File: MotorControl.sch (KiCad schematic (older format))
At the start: 2 parts, among them U3 74LVC125

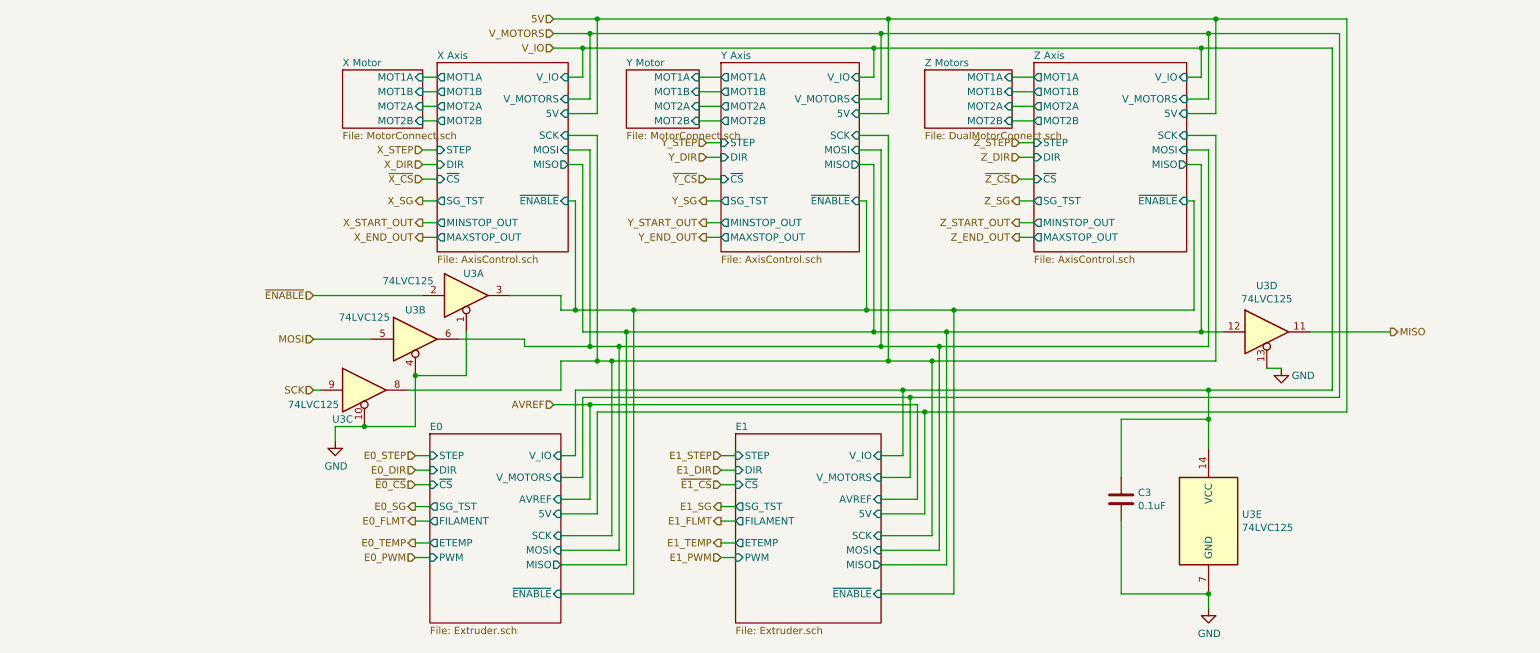
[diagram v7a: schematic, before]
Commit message: Added motor clock source.
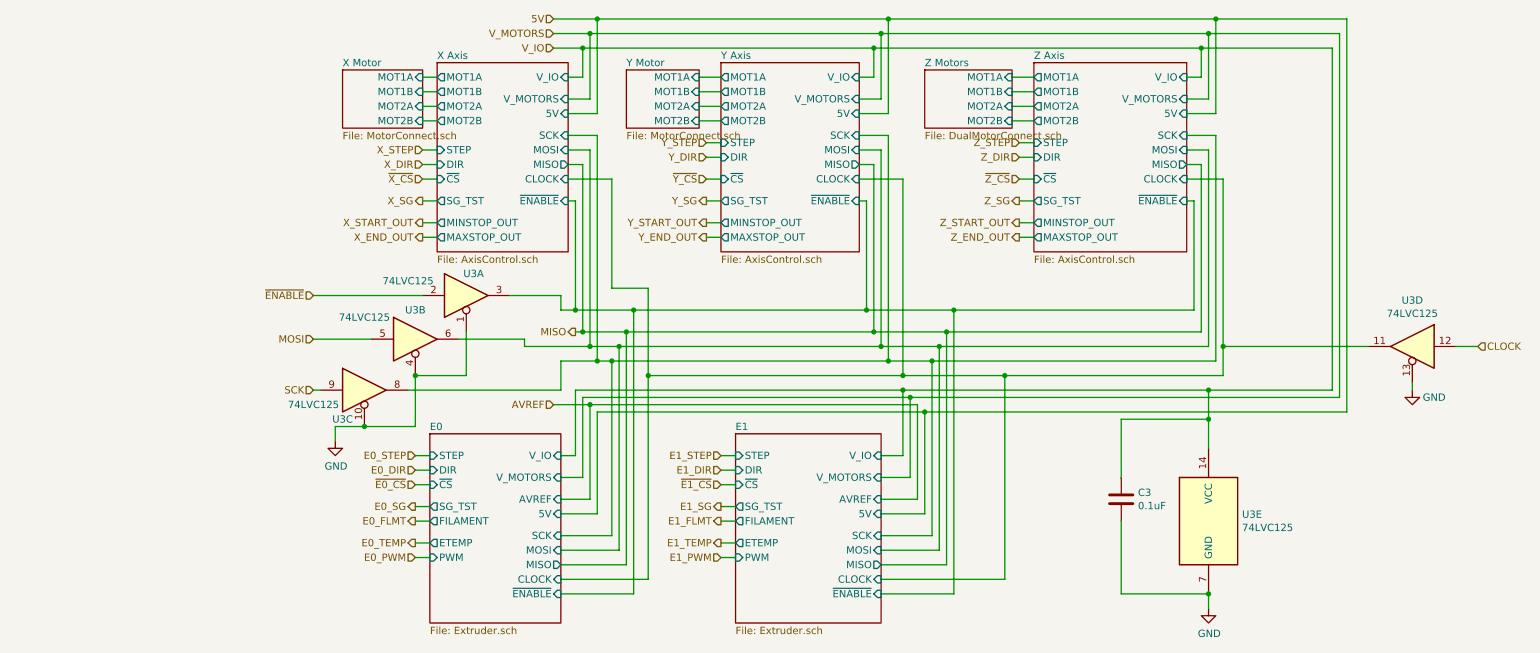
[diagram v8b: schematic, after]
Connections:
- net MISO: no longer U3.11
- net E0/MISO renamed CLOCK
- new net E0/CLOCK: U3.11
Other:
- moved on the sheet: U3D
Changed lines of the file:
@@
 F15 "PWM" I L 3350 4700 50
 F16 "5V" I R 4250 4400 50
+F17 "CLOCK" I R 4250 4850 50
 $EndSheet
 $Sheet
@@
 F17 "MINSTOP_OUT" O L 3400 2400 50
 F18 "5V" I R 4300 1650 50
+F19 "CLOCK" I R 4300 2100 50
 $EndSheet
 $Sheet
@@
 F17 "MINSTOP_OUT" O L 5350 2400 50
 F18 "5V" I R 6300 1650 50
+F19 "CLOCK" I R 6300 2100 50
 $EndSheet
 Wire Wire Line
@@
 Text HLabel 2550 2900 0    50   Input ~ 0
 ~ENABLE
-Text HLabel 9950 3150 2    50   Output ~ 0
+Text HLabel 4350 3150 0    50   Output ~ 0
 MISO
 Text HLabel 2550 3200 0    50   Input ~ 0
@@
 F17 "MINSTOP_OUT" O L 7500 2400 50
 F18 "5V" I R 8550 1650 50
+F19 "CLOCK" I R 8550 2100 50
 $EndSheet
 Wire Wire Line
@@
 F15 "PWM" I L 5450 4700 50
 F16 "5V" I R 6450 4400 50
+F17 "CLOCK" I R 6450 4850 50
 $EndSheet
 Wire Wire Line
@@
 L Logic_74xx:74LVC125 U3
 U 4 1 5AC4CBF3
-P 9100 3150
-F 0 "U3" H 9100 3467 50  0000 C CNN
-F 1 "74LVC125" H 9100 3376 50  0000 C CNN
-F 2 "Package_SO:TSSOP-14_4.4x5mm_P0.65mm" H 9100 3150 50  0001 C CNN
-F 3 "http://www.ti.com/lit/gpn/sn74LVC125" H 9100 3150 50  0001 C CNN
-	4    9100 3150
-	1    0    0    -1
+P 10100 3250
+F 0 "U3" H 10100 3567 50  0000 C CNN
+F 1 "74LVC125" H 10100 3476 50  0000 C CNN
+F 2 "Package_SO:TSSOP-14_4.4x5mm_P0.65mm" H 10100 3250 50  0001 C CNN
+F 3 "http://www.ti.com/lit/gpn/sn74LVC125" H 10100 3250 50  0001 C CNN
+	4    10100 3250
+	-1   0    0    -1
 $EndComp
 Wire Wire Line
@@
 Wire Wire Line
 	8700 1100 9600 1100
-Wire Wire Line
-	8650 3150 8800 3150
-Connection ~ 8650 3150
-Wire Wire Line
-	9400 3150 9950 3150
 $Comp
 L power:GND #PWR010
 U 1 1 5AC6FCE8
-P 9200 3400
-F 0 "#PWR010" H 9200 3150 50  0001 C CNN
-F 1 "GND" H 9350 3350 50  0000 C CNN
-F 2 "" H 9200 3400 50  0001 C CNN
-F 3 "" H 9200 3400 50  0001 C CNN
-	1    9200 3400
+P 10100 3550
+F 0 "#PWR010" H 10100 3300 50  0001 C CNN
+F 1 "GND" H 10250 3500 50  0000 C CNN
+F 2 "" H 10100 3550 50  0001 C CNN
+F 3 "" H 10100 3550 50  0001 C CNN
+	1    10100 3550
 	1    0    0    -1
 $EndComp
 Wire Wire Line
-	9100 3400 9200 3400
+	10100 3500 10100 3550
 $Comp
 L power:GND #PWR09
@@
 Wire Wire Line
 	4500 1000 6500 1000
+Wire Wire Line
+	4350 3150 4400 3150
+Connection ~ 4400 3150
+Wire Wire Line
+	4300 2100 4600 2100
+Wire Wire Line
+	4600 2100 4600 2850
+Wire Wire Line
+	4600 2850 4850 2850
+Wire Wire Line
+	4850 2850 4850 3450
+Wire Wire Line
+	4850 4850 4250 4850
+Wire Wire Line
+	6300 2100 6600 2100
+Wire Wire Line
+	6600 2100 6600 3450
+Wire Wire Line
+	6600 3450 4850 3450
+Connection ~ 4850 3450
+Wire Wire Line
+	4850 3450 4850 4850
+Wire Wire Line
+	8550 2100 8800 2100
+Wire Wire Line
+	8800 2100 8800 3250
+Wire Wire Line
+	8800 3450 7300 3450
+Connection ~ 6600 3450
+Wire Wire Line
+	6450 4850 7300 4850
+Wire Wire Line
+	7300 4850 7300 3450
+Connection ~ 7300 3450
+Wire Wire Line
+	7300 3450 6600 3450
+Wire Wire Line
+	9800 3250 8800 3250
+Connection ~ 8800 3250
+Wire Wire Line
+	8800 3250 8800 3450
+Text HLabel 10550 3250 2    50   Input ~ 0
+CLOCK
+Wire Wire Line
+	10550 3250 10400 3250
 $EndSCHEMATC
